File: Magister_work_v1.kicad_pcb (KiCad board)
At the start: 4 copper layers, 100 x 100 mm, 83 parts, among them J1 Conn_01x04_Pin, J10 Conn_01x02_Pin, J2 Conn_01x03_Pin, J3 Conn_01x03_Pin, J4 Conn_01x03_Pin, J5 Conn_01x03_Pin, J6 Conn_01x04_Pin, J7 Conn_01x04_Pin, J8 Conn_01x06_Pin, J9 Conn_01x02_Pin, U1 LM66100DCK, U2 XC6206P332MR, U3 Ai-Thinker-Ra-01, U4 MCP6001-OT, Y1 X322525MQB4SI

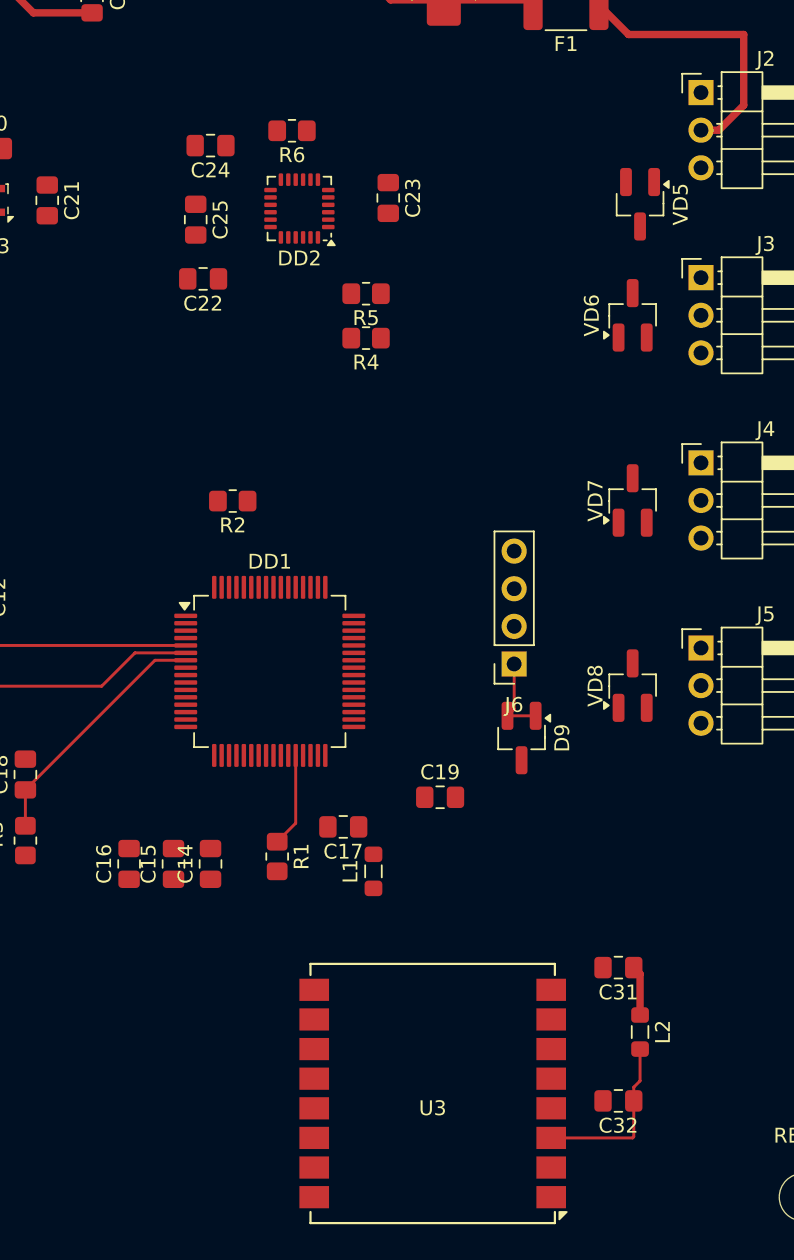
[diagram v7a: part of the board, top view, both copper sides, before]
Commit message: feat: added 3.3V line Power for Lora and sensors
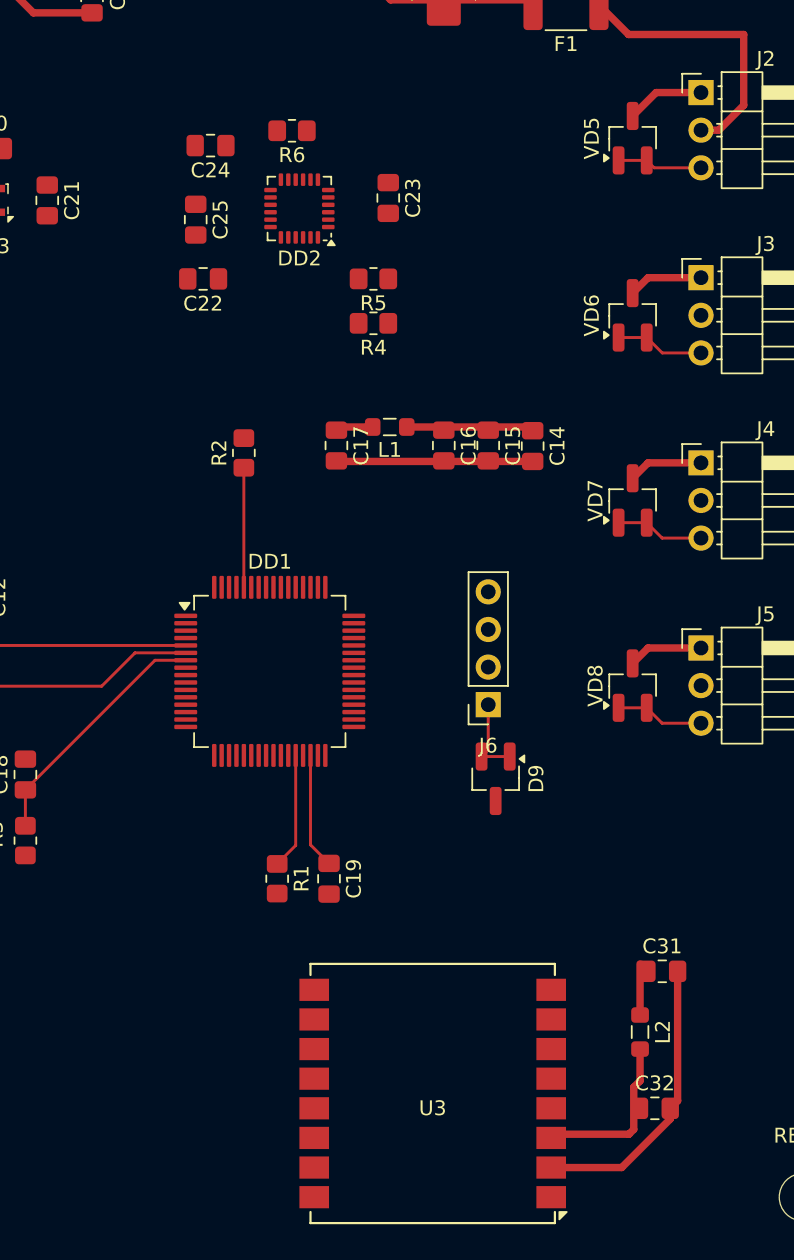
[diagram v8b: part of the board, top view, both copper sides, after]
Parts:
- moved C14 35.6 mm to (99.8, 67.8), turned to -90 degrees
- moved C15 35.4 mm to (96.8, 67.8), turned to -90 degrees
- moved C16 35.4 mm to (93.8, 67.8), turned to -90 degrees
- moved L1 30.0 mm to (90.1, 66.5), turned to 180 degrees
- moved C17 25.8 mm to (86.5, 67.8), turned to -90 degrees
- moved C19 9.30 mm to (86.0, 97.0), turned to -90 degrees
- moved VD5 4.49 mm to (106.5, 47.0), turned to 90 degrees
- moved R2 3.34 mm to (80.2, 68.2), turned to 90 degrees
- moved D9 3.26 mm to (97.2, 90.2)
- moved J6 3.26 mm to (96.8, 85.2)
- moved C31 2.97 mm to (108.5, 103.2), turned to 0 degrees
- moved C32 2.51 mm to (108.0, 112.5), turned to 0 degrees
- moved R1 1.50 mm to (82.5, 97.0)
- moved R4 1.12 mm to (89.0, 59.5)
- moved R5 1.12 mm to (89.0, 56.5)
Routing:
- net GND: track 173.8 -> 227.1 mm
- net +3V3D: track 16.8 -> 25.5 mm
- net Net-(DD1-BOOT0): track 0.00 -> 8.08 mm
- net Net-(DD1-VCAP1): track 0.00 -> 7.81 mm
- net PWM4: track 0.00 -> 6.00 mm
- net PWM3: track 0.00 -> 6.00 mm
- net PWM2: track 0.00 -> 6.00 mm
- net PWM1: track 0.00 -> 5.77 mm
- net +3V3_MCU: track 0.00 -> 2.71 mm
- net Net-(DD1-PB2): track 6.34 -> 7.84 mm
